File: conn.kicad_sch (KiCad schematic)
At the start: 59 parts

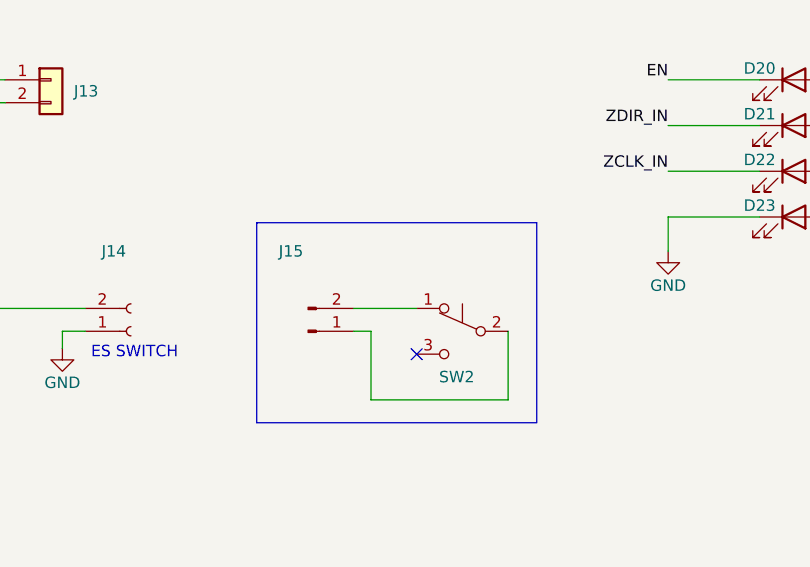
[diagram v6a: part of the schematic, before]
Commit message: Added 100n extra decoupling cap to PWM 12V reg.
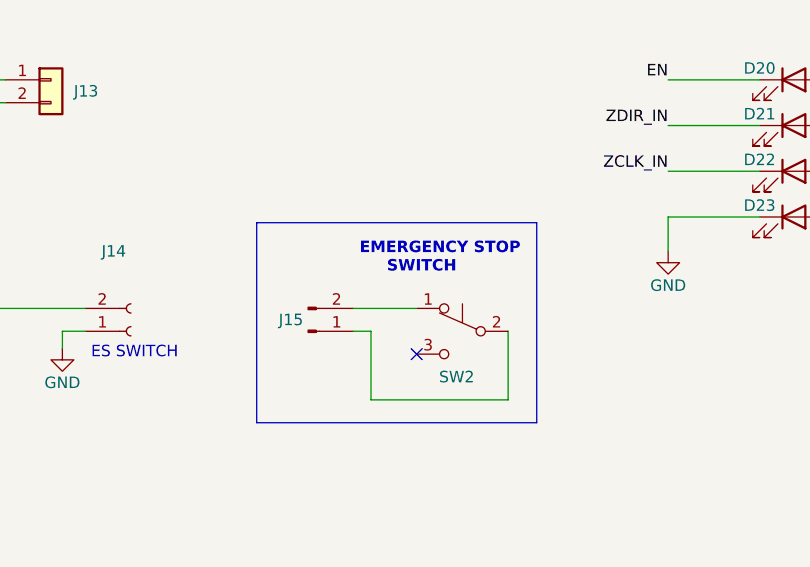
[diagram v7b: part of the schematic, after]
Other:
- note added: "EMERGENCY STOP SWITCH"
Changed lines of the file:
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@@
     (effects (font (size 1.27 1.27)) (justify left bottom))
+  )
+  (text "EMERGENCY STOP\n     SWITCH" (at 198.12 121.92 0)
+    (effects (font (size 1.27 1.27) (thickness 0.254) bold) (justify left bottom))
   )
   (text "_IN means \"into this sheet\"\n_OUT means \"out of this sheet\""
@@
   (symbol (lib_id "power:GND") (at 147.32 58.42 0) (unit 1)
     (in_bom yes) (on_board yes)
-    (property "Reference" "#PWR047" (id 0) (at 147.32 64.77 0)
+    (property "Reference" "#PWR046" (id 0) (at 147.32 64.77 0)
       (effects (font (size 1.27 1.27)) hide)
     )
@@
   (symbol (lib_id "power:GND") (at 67.31 118.11 0) (unit 1)
     (in_bom yes) (on_board yes)
-    (property "Reference" "#PWR042" (id 0) (at 67.31 124.46 0)
+    (property "Reference" "#PWR041" (id 0) (at 67.31 124.46 0)
       (effects (font (size 1.27 1.27)) hide)
     )
@@
   (symbol (lib_id "power:GND") (at 87.63 58.42 0) (unit 1)
     (in_bom yes) (on_board yes)
-    (property "Reference" "#PWR043" (id 0) (at 87.63 64.77 0)
+    (property "Reference" "#PWR042" (id 0) (at 87.63 64.77 0)
       (effects (font (size 1.27 1.27)) hide)
     )
@@
   (symbol (lib_id "power:+5V") (at 60.96 151.13 0) (unit 1)
     (in_bom yes) (on_board yes)
-    (property "Reference" "#PWR040" (id 0) (at 60.96 154.94 0)
+    (property "Reference" "#PWR039" (id 0) (at 60.96 154.94 0)
       (effects (font (size 1.27 1.27)) hide)
     )
@@
   (symbol (lib_id "power:GND") (at 232.41 86.36 0) (unit 1)
     (in_bom yes) (on_board yes)
-    (property "Reference" "#PWR054" (id 0) (at 232.41 92.71 0)
+    (property "Reference" "#PWR053" (id 0) (at 232.41 92.71 0)
       (effects (font (size 1.27 1.27)) hide)
     )
@@
   (symbol (lib_id "Connector:Conn_01x02_Male") (at 192.405 128.27 0) (mirror x) (unit 1)
     (in_bom no) (on_board no)
-    (property "Reference" "J15" (id 0) (at 190.5 119.38 0))
-    (property "Value" "" (id 1) (at 187.96 121.92 0)
-      (effects (font (size 1.27 1.27)) (justify left))
+    (property "Reference" "J15" (id 0) (at 190.5 127 0))
+    (property "Value" "" (id 1) (at 193.04 130.81 0)
+      (effects (font (size 1.27 1.27)) (justify left) hide)
     )
     (property "Footprint" "" (id 2) (at 192.405 128.27 0)
@@
   (symbol (lib_id "power:GND") (at 116.84 58.42 0) (unit 1)
     (in_bom yes) (on_board yes)
-    (property "Reference" "#PWR045" (id 0) (at 116.84 64.77 0)
+    (property "Reference" "#PWR044" (id 0) (at 116.84 64.77 0)
       (effects (font (size 1.27 1.27)) hide)
     )
@@
   (symbol (lib_id "power:GND") (at 232.41 119.38 0) (unit 1)
     (in_bom yes) (on_board yes)
-    (property "Reference" "#PWR055" (id 0) (at 232.41 125.73 0)
+    (property "Reference" "#PWR054" (id 0) (at 232.41 125.73 0)
       (effects (font (size 1.27 1.27)) hide)
     )
@@
   (symbol (lib_id "power:GND") (at 187.96 73.66 0) (unit 1)
     (in_bom yes) (on_board yes)
-    (property "Reference" "#PWR052" (id 0) (at 187.96 80.01 0)
+    (property "Reference" "#PWR051" (id 0) (at 187.96 80.01 0)
       (effects (font (size 1.27 1.27)) hide)
     )
@@
   (symbol (lib_id "power:GND") (at 60.96 178.435 0) (unit 1)
     (in_bom yes) (on_board yes)
-    (property "Reference" "#PWR041" (id 0) (at 60.96 184.785 0)
+    (property "Reference" "#PWR040" (id 0) (at 60.96 184.785 0)
       (effects (font (size 1.27 1.27)) hide)
     )
@@
   (symbol (lib_id "power:+5V") (at 116.84 33.02 0) (unit 1)
     (in_bom yes) (on_board yes)
-    (property "Reference" "#PWR044" (id 0) (at 116.84 36.83 0)
+    (property "Reference" "#PWR043" (id 0) (at 116.84 36.83 0)
       (effects (font (size 1.27 1.27)) hide)
     )
@@
   (symbol (lib_id "power:GND") (at 165.1 130.175 0) (unit 1)
     (in_bom yes) (on_board yes)
-    (property "Reference" "#PWR048" (id 0) (at 165.1 136.525 0)
+    (property "Reference" "#PWR047" (id 0) (at 165.1 136.525 0)
       (effects (font (size 1.27 1.27)) hide)
     )
@@
   (symbol (lib_id "power:GND") (at 231.14 53.34 0) (unit 1)
     (in_bom yes) (on_board yes)
-    (property "Reference" "#PWR053" (id 0) (at 231.14 59.69 0)
+    (property "Reference" "#PWR052" (id 0) (at 231.14 59.69 0)
       (effects (font (size 1.27 1.27)) hide)
     )
@@
     (property "Reference" "SW2" (id 0) (at 208.915 133.35 0))
     (property "Value" "" (id 1) (at 209.55 122.555 0)
-      (effects (font (size 1.27 1.27) bold))
+      (effects (font (size 1.27 1.27) bold) hide)
     )
     (property "Footprint" "" (id 2) (at 209.55 128.27 0)
@@
   (symbol (lib_id "power:+5V") (at 118.11 73.66 0) (unit 1)
     (in_bom yes) (on_board yes)
-    (property "Reference" "#PWR046" (id 0) (at 118.11 77.47 0)
+    (property "Reference" "#PWR045" (id 0) (at 118.11 77.47 0)
       (effects (font (size 1.27 1.27)) hide)
     )
@@
   (symbol (lib_id "power:GND") (at 187.96 49.53 0) (unit 1)
     (in_bom yes) (on_board yes)
-    (property "Reference" "#PWR051" (id 0) (at 187.96 55.88 0)
+    (property "Reference" "#PWR050" (id 0) (at 187.96 55.88 0)
       (effects (font (size 1.27 1.27)) hide)
     )
@@
   (symbol (lib_id "power:+5V") (at 179.07 39.37 0) (unit 1)
     (in_bom yes) (on_board yes)
-    (property "Reference" "#PWR049" (id 0) (at 179.07 43.18 0)
+    (property "Reference" "#PWR048" (id 0) (at 179.07 43.18 0)
       (effects (font (size 1.27 1.27)) hide)
     )
@@
   (symbol (lib_id "power:+5V") (at 179.07 63.5 0) (unit 1)
     (in_bom yes) (on_board yes)
-    (property "Reference" "#PWR050" (id 0) (at 179.07 67.31 0)
-      (effects (font (size 1.27 1.27)) hide)
-    )
+    (property "Reference" "#PWR049" (id 0) (at 179.07 67.31 0)
+      (effects (font (size 1.27 1.27)) hide)
+    )

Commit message: I'm soooo done with this board! :/
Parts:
- D10, D11, D15, D19, D23, D8, D9: value (none) -> RED; footprint (none) -> -Project:LED_0402_DOT; JLCMFR# (none) -> NCD0402R1; JLCMOQ (none) -> 20; JLCPART (none) -> C130719
- D12, D16, D20: value (none) -> GRN; footprint (none) -> -Project:LED_0402_DOT; JLCMFR# (none) -> NCD0402G1; JLCMOQ (none) -> 20; JLCPART (none) -> C130723
- D13, D17, D21: value (none) -> ORG; footprint (none) -> -Project:LED_0402_DOT; JLCMFR# (none) -> NCD0402O1; JLCMOQ (none) -> 20; JLCPART (none) -> C130720
- D14, D18, D22: value (none) -> BLU; footprint (none) -> -Project:LED_0402_DOT; JLCMFR# (none) -> NCD0402B1; JLCMOQ (none) -> 20; JLCPART (none) -> C130724
- J10, J12, J7: value (none) -> MicroFit_2x04; footprint (none) -> Connector_Molex:Molex_Micro-Fit_3.0_43045-0812_2x04_P3.00mm_Vertical; JLCMFR# (none) -> DNI
- J11, J6, J8, J9: value (none) -> JST_1x04; footprint (none) -> Connector_JST:JST_EH_S4B-EH_1x04_P2.50mm_Horizontal; JLCMFR# (none) -> S4B-XH-A(LF)(SN); JLCMOQ (none) -> 2; JLCPART (none) -> C157925
- J13: value (none) -> JST_01x02; footprint (none) -> Connector_JST:JST_EH_B2B-EH-A_1x02_P2.50mm_Vertical; JLCMFR# (none) -> B2B-XH-A(LF)(SN); JLCMOQ (none) -> 2; JLCPART (none) -> C158012; LCSC C161869 -> (none); LCSCMFR# B2B-XH-AM(LF)(SN) -> (none)
- J14: value (none) -> JST_1x02; footprint (none) -> Connector_JST:JST_EH_S2B-EH_1x02_P2.50mm_Horizontal; E14MFR# S2B-XH-A-1(LF)(SN) -> (none); JLCMFR# (none) -> S2B-XH-A(LF)(SN); JLCMOQ (none) -> 2; JLCPART (none) -> C157931; LCSC C163035 -> (none)
- J15, SW2: value (none) -> DNI; JLCMFR# (none) -> DNI
- J16, J17: value (none) -> MLX_1x03; footprint (none) -> Connector_Molex:Molex_KK-254_AE-6410-03A_1x03_P2.54mm_Vertical; JLCMFR# (none) -> DNI
- J5: value (none) -> JST_B6B-XH; footprint (none) -> Connector_JST:JST_EH_S6B-EH_1x06_P2.50mm_Horizontal; E14MOQ (none) -> 100; JLCMFR# (none) -> S6B-XH-A(LF)(SN); JLCMOQ (none) -> 2; JLCPART (none) -> C157919; MOQ 100 -> (none)
- LF1: value (none) -> SRF0905A-472Y; footprint (none) -> Filter:Filter_Bourns_SRF0905_6.0x9.2mm; E14MOQ (none) -> 1; JLCMFR# (none) -> SRF0905A-472Y; JLCMOQ (none) -> 2; JLCPART (none) -> C113524; MOQ 1 -> (none)
- NT10, NT11, NT12, NT13, NT14, NT15, NT16, NT17, NT18, NT19, NT20, NT21, NT22, NT23, NT26, NT27, NT4, NT5, NT6, NT7, NT9: value (none) -> DNI; footprint (none) -> -Project:NetTie-2_SMD_Pad0.3mm; JLCMFR# (none) -> DNI
- NT24, NT25, NT8: value (none) -> DNI; footprint (none) -> -Project:NetTie-2_SMD_Pad1.0mm; JLCMFR# (none) -> DNI
- RN5, RN6, RN7, RN8: value (none) -> 1Kx4; footprint (none) -> Resistor_SMD:R_Array_Convex_4x0603; E14MOQ (none) -> 1; JLCMFR# (none) -> 4D03WGJ0102T5E; JLCMOQ (none) -> 20; JLCPART (none) -> C20197; LCSC C20197 -> (none); LCSCMFR# 4D03WGJ0102T5E -> (none); MOQ 1 -> (none)
